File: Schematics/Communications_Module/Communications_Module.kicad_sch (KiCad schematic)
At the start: 51 parts, among them J1 USB_B_Micro, J2 Bus_PCI_Express_x1, J3 Conn_01x04_Pin, Q1 NMOS, SW1 Boot Mode, U1 RFM95W-915S2, U10 WS2811, U2 W25Q128JVSIQ, U3 AMS1117-3.3, U4 LM66100DCKR, U5 LM66100DCKR, U6 LM66100DCKR, U7 STM32F103CBTx, U8 ACS706xLC-05C, U9 ISO1042BQDWVQ1, Y1 X322516MMB4SI

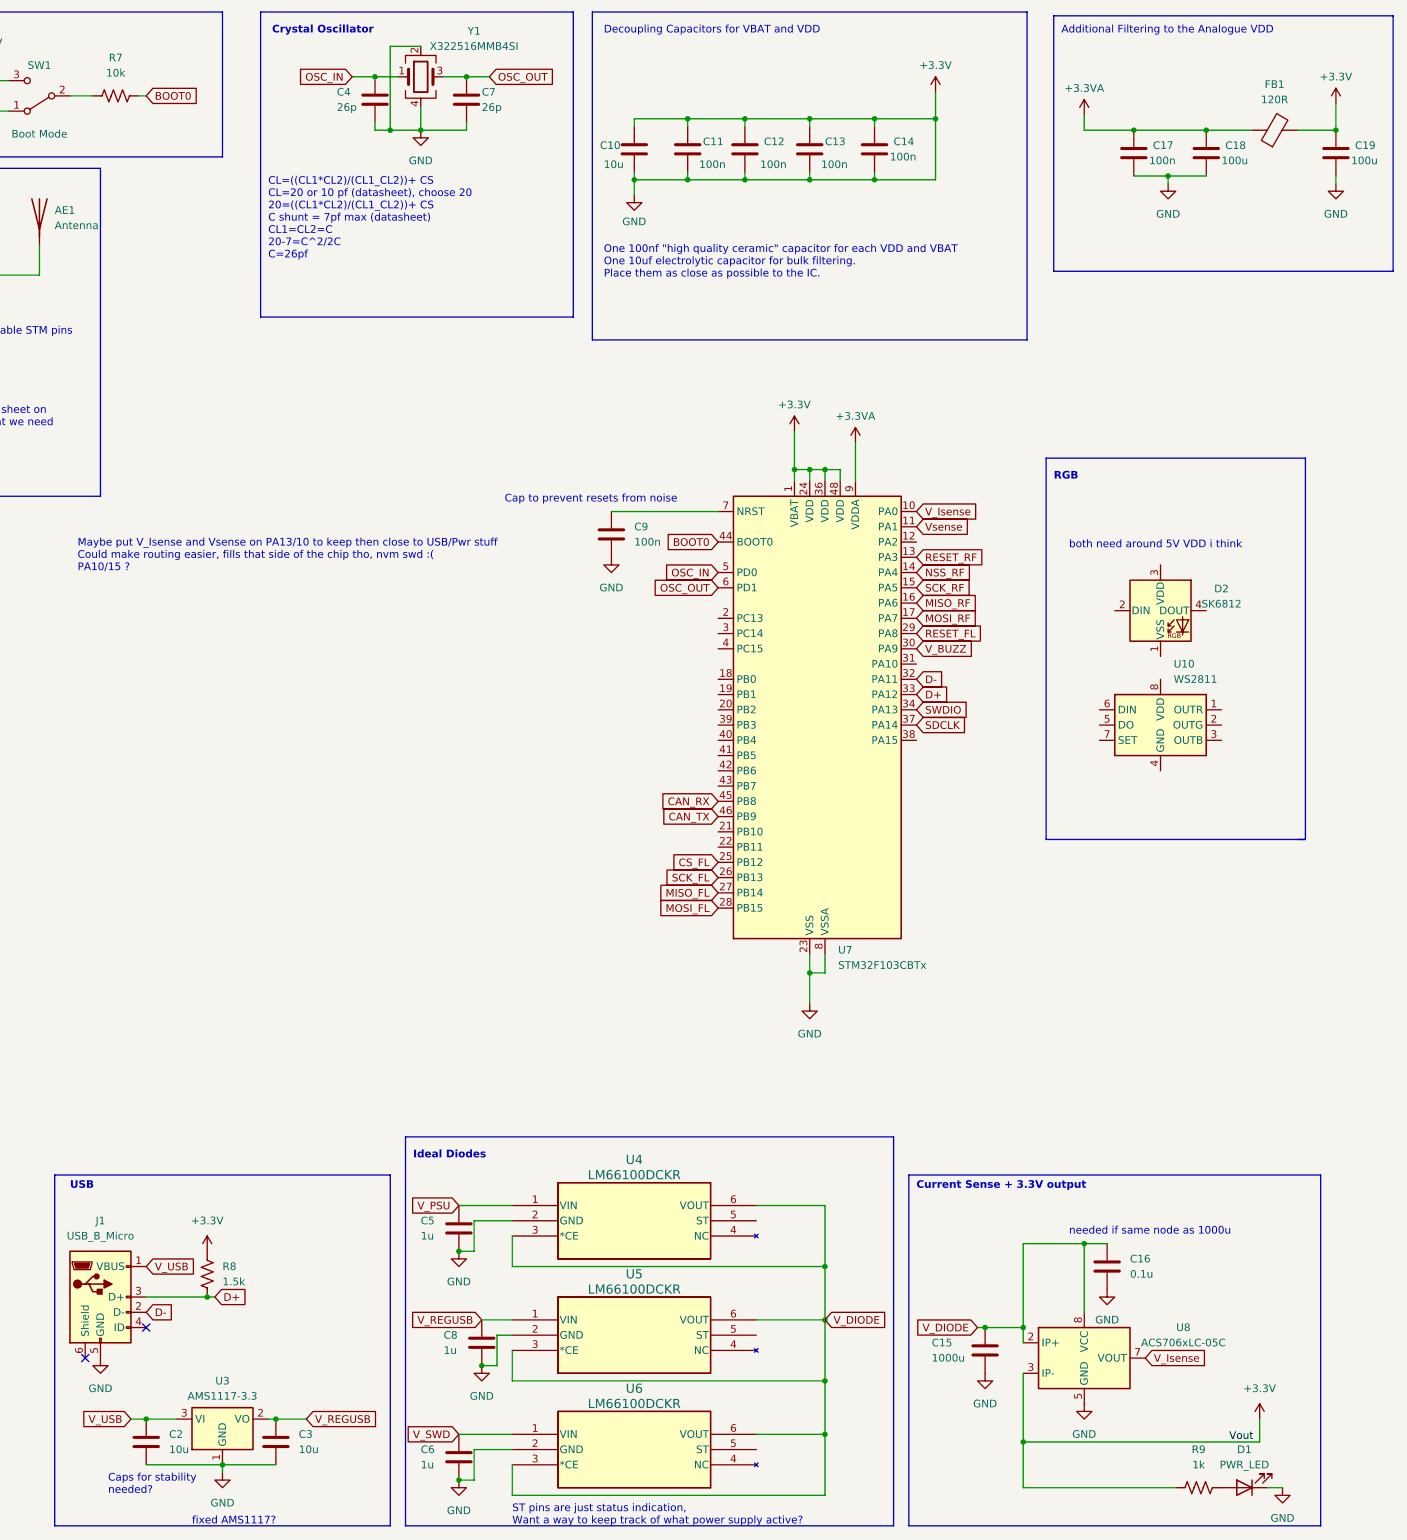
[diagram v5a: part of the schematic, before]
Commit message: Added correct RGB symbol, added/clarified some notes & questions on schematic.
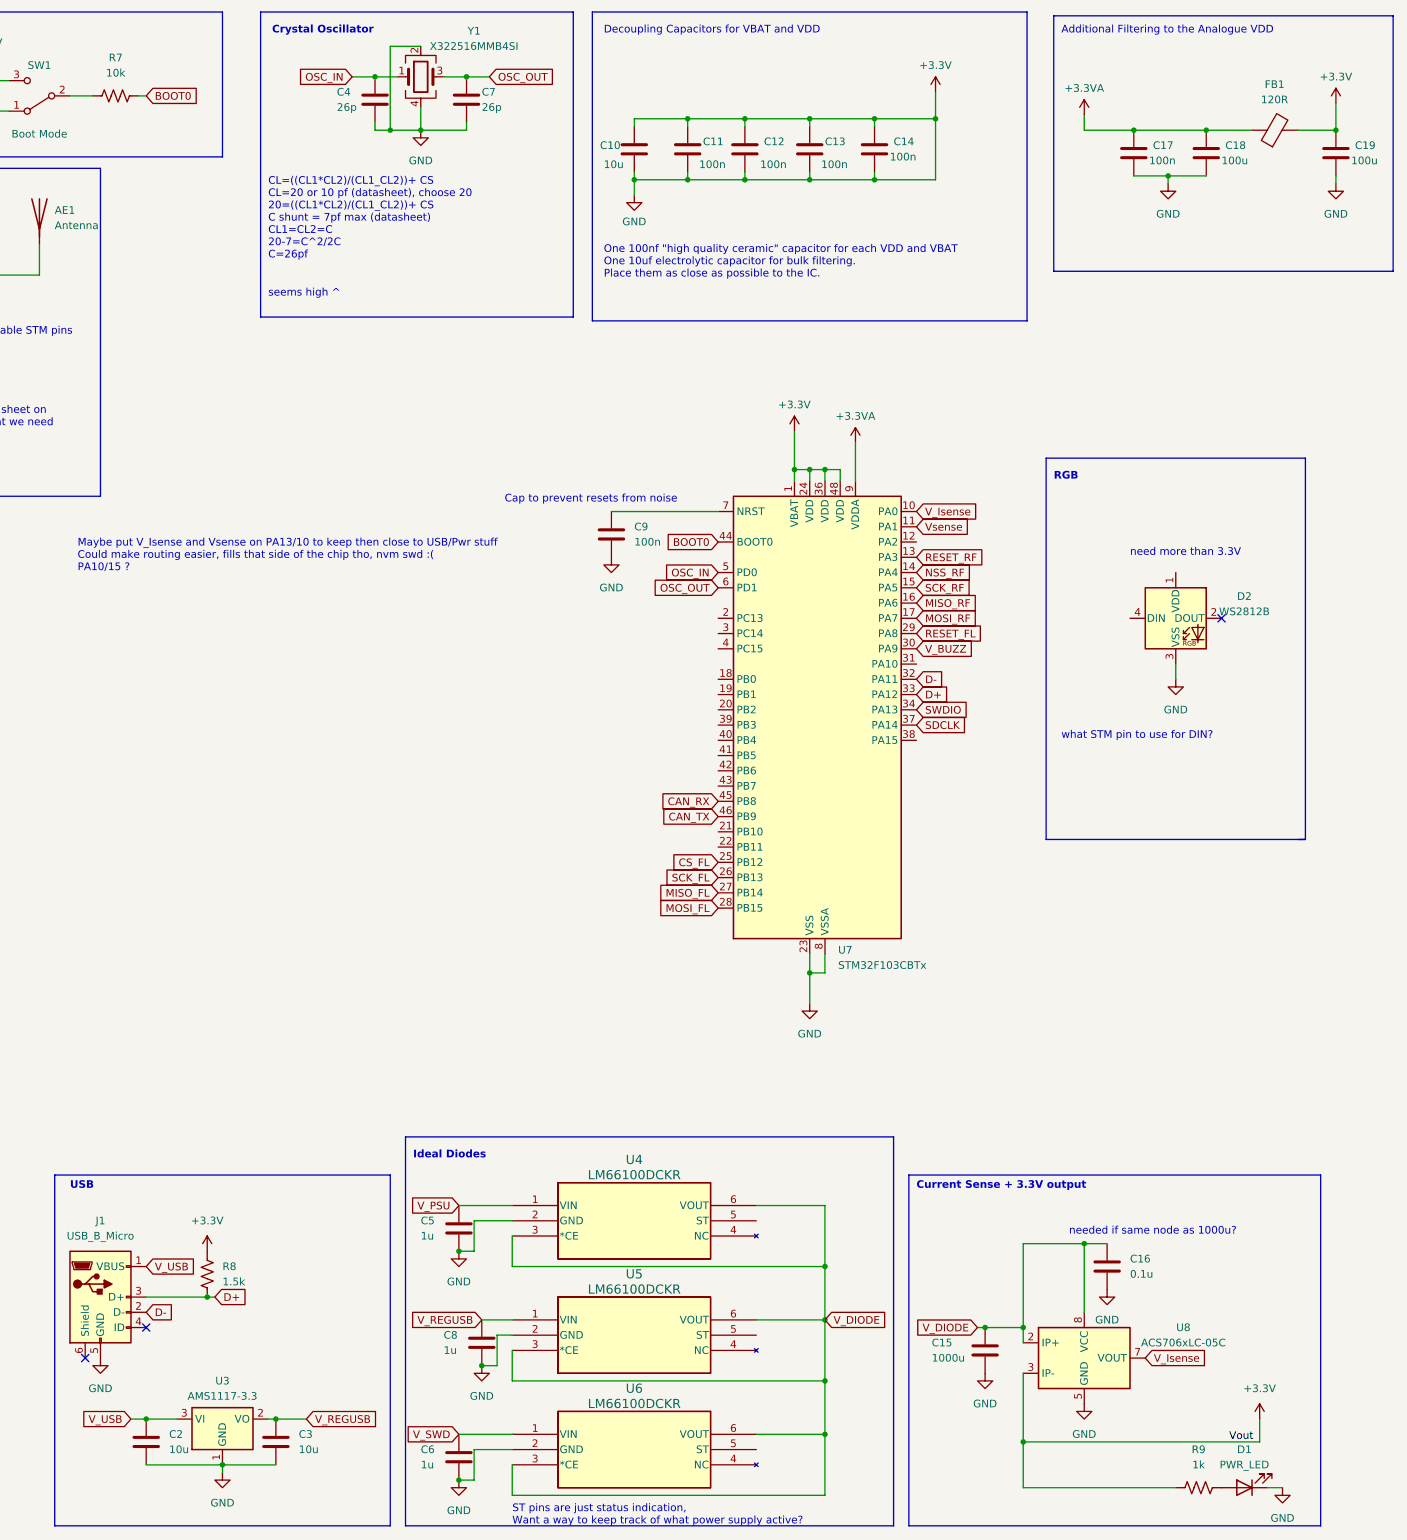
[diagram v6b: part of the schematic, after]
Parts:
- removed D2: SK6812, LED_SMD:LED_SK6812_PLCC4_5.0x5.0mm_P3.2mm, symbol LED:SK6812
- removed U10: WS2811, symbol Driver_LED:WS2811
- added D2: WS2812B, LED_SMD:LED_WS2812B_PLCC4_5.0x5.0mm_P3.2mm, symbol LED:WS2812B
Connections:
- net +3.3V: now also D2.3 (VSS)
- no-connect marks 2 -> 3
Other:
- note added: "need more than 3.3V"
- note added: "needed if same node as 1000u?"
- note added: "seems high ^"
- note added: "what STM pin to use for DIN?"
- note removed: "Caps for stability needed?"
- note removed: "both need around 5V VDD i think"
- note removed: "fixed AMS1117?"
- note removed: "needed if same node as 1000u"
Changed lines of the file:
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@@
   (title_block
     (title "QRET 23-24 SRAD Communications Module")
-    (date "2024-01-26")
-    (rev "V0.2.1")
+    (date "2024-01-31")
+    (rev "V0.2.2")
     (company "Queen's Rocket Engineering Team")
     (comment 1 "Contributors: Oak Campbell")
@@
   (junction (at 170.18 238.76) (diameter 0) (color 0 0 0 0)
   )
+  (no_connect (at 293.37 114.3))
   (no_connect (at 104.14 237.49))
   (no_connect (at 114.3 232.41))
@@
     (stroke (width 0) (type default))
   )
+  (wire (pts (xy 285.75 121.92) (xy 285.75 124.46))
+    (stroke (width 0) (type default))
+  )
   (wire (pts (xy 254 232.41) (xy 260.35 232.41))
     (stroke (width 0) (type default))
@@
     (fill (type none))
   )
-  (rectangle (start 188.595 13.335) (end 260.985 67.945)
+  (rectangle (start 188.595 13.335) (end 260.985 64.77)
     (stroke (width 0) (type default))
     (fill (type none))
@@
     (effects (font (size 1.27 1.27)) (justify left bottom))
   )
+  (text "seems high ^" (at 134.62 60.96 0)
+    (effects (font (size 1.27 1.27)) (justify left bottom))
+  )
   (text "Crystal Oscillator" (at 135.255 17.145 0)
     (effects (font (size 1.27 1.27) (thickness 0.254) bold) (justify left bottom))
@@
     (effects (font (size 1.27 1.27) (thickness 0.254) bold) (justify left bottom))
   )
-  (text "Also SPI no ic2" (at 35.56 101.6 0)
+  (text "need more than 3.3V" (at 278.13 104.14 0)
     (effects (font (size 1.27 1.27)) (justify left bottom))
   )
-  (text "fixed AMS1117?" (at 121.92 265.43 0)
+  (text "Also SPI no ic2" (at 35.56 101.6 0)
     (effects (font (size 1.27 1.27)) (justify left bottom))
   )
@@
     (effects (font (size 1.27 1.27)) (justify left bottom))
   )
-  (text "both need around 5V VDD i think" (at 267.97 102.87 0)
-    (effects (font (size 1.27 1.27)) (justify left bottom))
-  )
   (text "Current Sense + 3.3V output" (at 242.57 209.55 0)
     (effects (font (size 1.27 1.27) (thickness 0.254) bold) (justify left bottom))
@@
     (effects (font (size 1.27 1.27) (thickness 0.254) bold) (justify left bottom))
   )
+  (text "what STM pin to use for DIN?" (at 266.7 134.62 0)
+    (effects (font (size 1.27 1.27)) (justify left bottom))
+  )
   (text "RF" (at 16.51 43.18 0)
     (effects (font (size 1.27 1.27) bold) (justify left bottom))
   )
-  (text "Caps for stability\nneeded?" (at 107.95 260.35 0)
-    (effects (font (size 1.27 1.27)) (justify left bottom))
-  )
-  (text "needed if same node as 1000u" (at 267.97 217.17 0)
+  (text "needed if same node as 1000u?" (at 267.97 217.17 0)
     (effects (font (size 1.27 1.27)) (justify left bottom))
   )
@@
     )
   )
-  (symbol (lib_id "LED:SK6812") (at 283.21 113.03 0) (unit 1)
-    (in_bom yes) (on_board yes) (dnp no) (fields_autoplaced)
-    (property "Reference" "D2" (at 293.37 109.3821 0)
-      (effects (font (size 1.27 1.27)))
-    )
-    (property "Value" "SK6812" (at 293.37 111.9221 0)
-      (effects (font (size 1.27 1.27)))
-    )
-    (property "Footprint" "LED_SMD:LED_SK6812_PLCC4_5.0x5.0mm_P3.2mm" (at 284.48 120.65 0)
-      (effects (font (size 1.27 1.27)) (justify left top) hide)
-    )
-    (property "Datasheet" "https://cdn-shop.adafruit.com/product-files/1138/SK6812+LED+datasheet+.pdf" (at 285.75 122.555 0)
-      (effects (font (size 1.27 1.27)) (justify left top) hide)
-    )
-    (pin "1")
-    (pin "2")
-    (pin "3")
-    (pin "4")
-    (instances
-      (project "Communications_Module"
-        (path "/ace06731-9b48-45c3-868d-c65fed1a8f9b"
-          (reference "D2") (unit 1)
-        )
-      )
-    )
-  )
   (symbol (lib_id "power:GND") (at 72.39 113.03 0) (unit 1)
     (in_bom yes) (on_board yes) (dnp no) (fields_autoplaced)
@@
     )
   )
-  (symbol (lib_id "Driver_LED:WS2811") (at 283.21 132.08 0) (unit 1)
-    (in_bom yes) (on_board yes) (dnp no) (fields_autoplaced)
-    (property "Reference" "U10" (at 285.4041 121.92 0)
-      (effects (font (size 1.27 1.27)) (justify left))
-    )
-    (property "Value" "WS2811" (at 285.4041 124.46 0)
-      (effects (font (size 1.27 1.27)) (justify left))
-    )
-    (property "Footprint" "" (at 275.59 128.27 0)
-      (effects (font (size 1.27 1.27)) hide)
-    )
-    (property "Datasheet" "https://cdn-shop.adafruit.com/datasheets/WS2811.pdf" (at 278.13 125.73 0)
-      (effects (font (size 1.27 1.27)) hide)
-    )
-    (pin "1")
-    (pin "2")
-    (pin "3")
-    (pin "4")
-    (pin "5")
-    (pin "6")
-    (pin "7")
-    (pin "8")
-    (instances
-      (project "Communications_Module"
-        (path "/ace06731-9b48-45c3-868d-c65fed1a8f9b"
-          (reference "U10") (unit 1)
-        )
-      )
-    )
-  )
   (symbol (lib_id "power:GND2") (at 403.86 30.48 180) (unit 1)
     (in_bom yes) (on_board yes) (dnp no) (fields_autoplaced)
@@
     )
   )
+  (symbol (lib_id "LED:WS2812B") (at 285.75 114.3 0) (unit 1)
+    (in_bom yes) (on_board yes) (dnp no) (fields_autoplaced)
+    (property "Reference" "D2" (at 297.18 110.6521 0)
+      (effects (font (size 1.27 1.27)))
+    )
+    (property "Value" "WS2812B" (at 297.18 113.1921 0)
+      (effects (font (size 1.27 1.27)))
+    )
+    (property "Footprint" "LED_SMD:LED_WS2812B_PLCC4_5.0x5.0mm_P3.2mm" (at 287.02 121.92 0)
+      (effects (font (size 1.27 1.27)) (justify left top) hide)
+    )
+    (property "Datasheet" "https://cdn-shop.adafruit.com/datasheets/WS2812B.pdf" (at 288.29 123.825 0)
+      (effects (font (size 1.27 1.27)) (justify left top) hide)
+    )
+    (pin "1")
+    (pin "2")
+    (pin "3")
+    (pin "4")
+    (instances
+      (project "Communications_Module"
+        (path "/ace06731-9b48-45c3-868d-c65fed1a8f9b"
+          (reference "D2") (unit 1)
+        )
+      )
+    )
+  )
   (symbol (lib_id "Device:C") (at 278.765 36.83 0) (unit 1)
     (in_bom yes) (on_board yes) (dnp no)
@@
         )
       )
+    )
+  )
+  (symbol (lib_id "power:GND") (at 285.75 124.46 0) (unit 1)
+    (in_bom yes) (on_board yes) (dnp no) (fields_autoplaced)
+    (property "Reference" "#PWR041" (at 285.75 130.81 0)
+      (effects (font (size 1.27 1.27)) hide)
+    )
+    (property "Value" "GND" (at 285.75 129.54 0)
+      (effects (font (size 1.27 1.27)))
+    )
+    (property "Footprint" "" (at 285.75 124.46 0)
+      (effects (font (size 1.27 1.27)) hide)
+    )
+    (property "Datasheet" "" (at 285.75 124.46 0)
+      (effects (font (size 1.27 1.27)) hide)
+    )
+    (pin "1")
+    (instances
+      (project "Communications_Module"
+        (path "/ace06731-9b48-45c3-868d-c65fed1a8f9b"
+          (reference "#PWR041") (unit 1)
+        )
+      )
